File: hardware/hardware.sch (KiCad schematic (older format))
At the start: 38 parts, among them J1 USB_B_Micro, J2 Breakout, Q1 FS8205, U1 USBLC6-2, U2 PIC18F45K50_QFP, U3 LM317A, U4 DW01+G, U5 TP4056

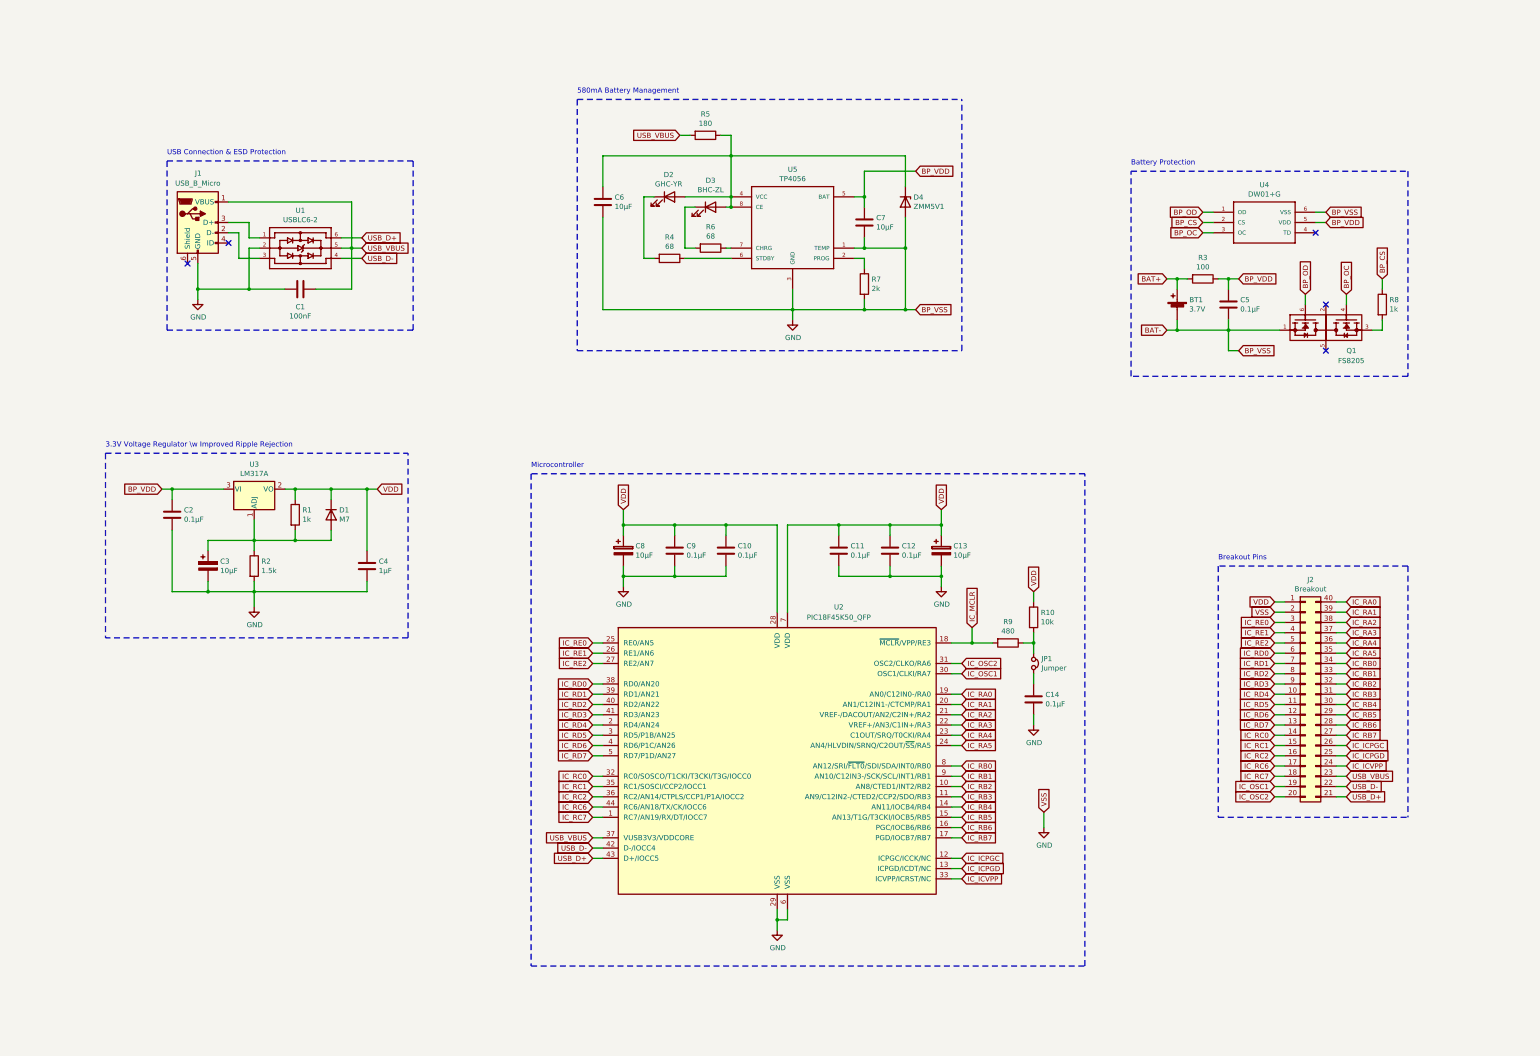
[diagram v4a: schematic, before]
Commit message: Assigned footprints to the project.
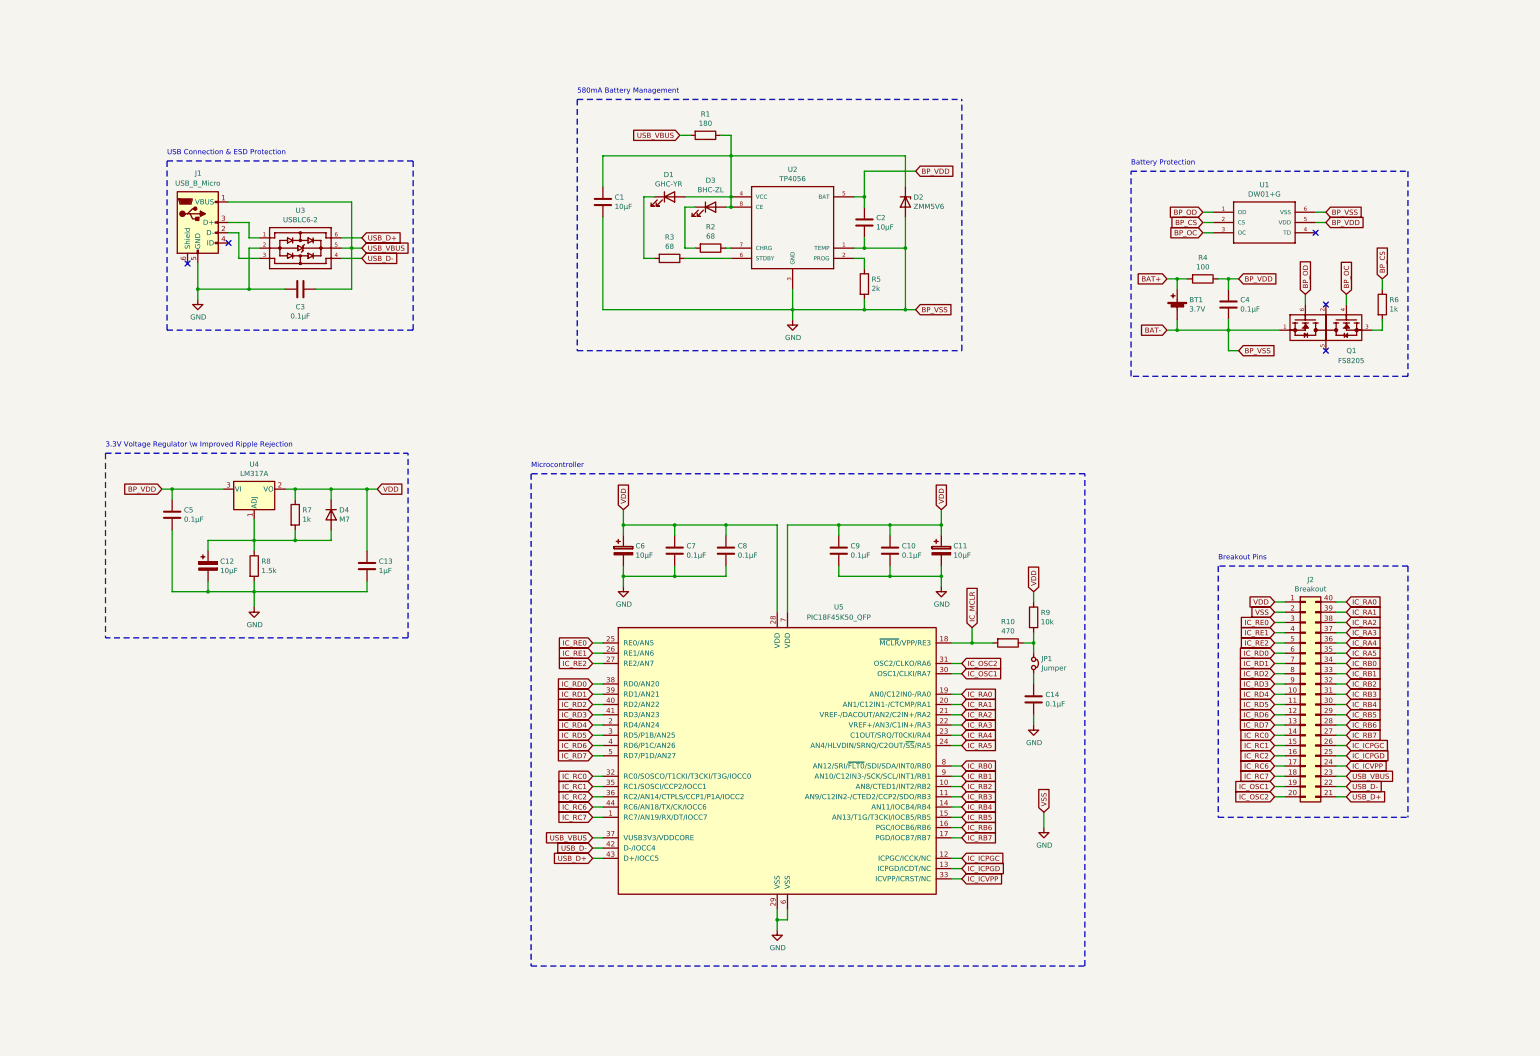
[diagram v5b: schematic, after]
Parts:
- BT1: footprint (none) -> Connector_PinHeader_2.54mm:PinHeader_1x02_P2.54mm_Horizontal
- C1: renamed from C6; footprint (none) -> Capacitor_SMD:C_0603_1608Metric_Pad1.05x0.95mm_HandSolder
- C10: renamed from C12; footprint (none) -> Capacitor_SMD:C_0603_1608Metric_Pad1.05x0.95mm_HandSolder
- C11: renamed from C13; footprint (none) -> Capacitor_SMD:C_0603_1608Metric_Pad1.05x0.95mm_HandSolder
- C12: renamed from C3; footprint (none) -> Capacitor_SMD:C_0603_1608Metric_Pad1.05x0.95mm_HandSolder
- C13: renamed from C4; footprint (none) -> Capacitor_SMD:C_0603_1608Metric_Pad1.05x0.95mm_HandSolder
- C14: footprint (none) -> Capacitor_SMD:C_0603_1608Metric_Pad1.05x0.95mm_HandSolder
- C2: renamed from C7; footprint (none) -> Capacitor_SMD:C_0603_1608Metric_Pad1.05x0.95mm_HandSolder
- C3: renamed from C1; value 100nF -> 0.1μF; footprint (none) -> Capacitor_SMD:C_0603_1608Metric_Pad1.05x0.95mm_HandSolder
- C4: renamed from C5; footprint (none) -> Capacitor_SMD:C_0603_1608Metric_Pad1.05x0.95mm_HandSolder
- C5: renamed from C2; footprint (none) -> Capacitor_SMD:C_0603_1608Metric_Pad1.05x0.95mm_HandSolder
- C6: renamed from C8; footprint (none) -> Capacitor_SMD:C_0603_1608Metric_Pad1.05x0.95mm_HandSolder
- C7: renamed from C9; footprint (none) -> Capacitor_SMD:C_0603_1608Metric_Pad1.05x0.95mm_HandSolder
- C8: renamed from C10; footprint (none) -> Capacitor_SMD:C_0603_1608Metric_Pad1.05x0.95mm_HandSolder
- C9: renamed from C11; footprint (none) -> Capacitor_SMD:C_0603_1608Metric_Pad1.05x0.95mm_HandSolder
- D1: renamed from D2; footprint (none) -> LED_SMD:LED_0603_1608Metric_Pad1.05x0.95mm_HandSolder
- D2: renamed from D4; value ZMM5V1 -> ZMM5V6
- D3: footprint (none) -> LED_SMD:LED_0603_1608Metric_Pad1.05x0.95mm_HandSolder
- D4: renamed from D1; footprint (none) -> Diode_SMD:D_MiniMELF_Handsoldering
- J1: footprint (none) -> Connector_USB:USB_Micro-B_Molex_47346-0001
- J2: footprint (none) -> Connector_PinHeader_2.54mm:PinHeader_2x20_P2.54mm_Vertical
- JP1: footprint (none) -> Connector_PinHeader_2.54mm:PinHeader_1x02_P2.54mm_Vertical
- R1: renamed from R5; footprint (none) -> Resistor_SMD:R_0603_1608Metric_Pad1.05x0.95mm_HandSolder
- R10: renamed from R9; value 480 -> 470; footprint (none) -> Resistor_SMD:R_0603_1608Metric_Pad1.05x0.95mm_HandSolder
- R2: renamed from R6; footprint (none) -> Resistor_SMD:R_0603_1608Metric_Pad1.05x0.95mm_HandSolder
- R3: renamed from R4; footprint (none) -> Resistor_SMD:R_0603_1608Metric_Pad1.05x0.95mm_HandSolder
- R4: renamed from R3; footprint (none) -> Resistor_SMD:R_0603_1608Metric_Pad1.05x0.95mm_HandSolder
- R5: renamed from R7; footprint (none) -> Resistor_SMD:R_0603_1608Metric_Pad1.05x0.95mm_HandSolder
- R6: renamed from R8; footprint (none) -> Resistor_SMD:R_0603_1608Metric_Pad1.05x0.95mm_HandSolder
- R7: renamed from R1; footprint (none) -> Resistor_SMD:R_0603_1608Metric_Pad1.05x0.95mm_HandSolder
- R8: renamed from R2; footprint (none) -> Resistor_SMD:R_0603_1608Metric_Pad1.05x0.95mm_HandSolder
- R9: renamed from R10; footprint (none) -> Resistor_SMD:R_0603_1608Metric_Pad1.05x0.95mm_HandSolder
- renumbered U4 to U1, U5 to U2, U1 to U3, U3 to U4, U2 to U5

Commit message: MAX2871 datasheet & footprint.
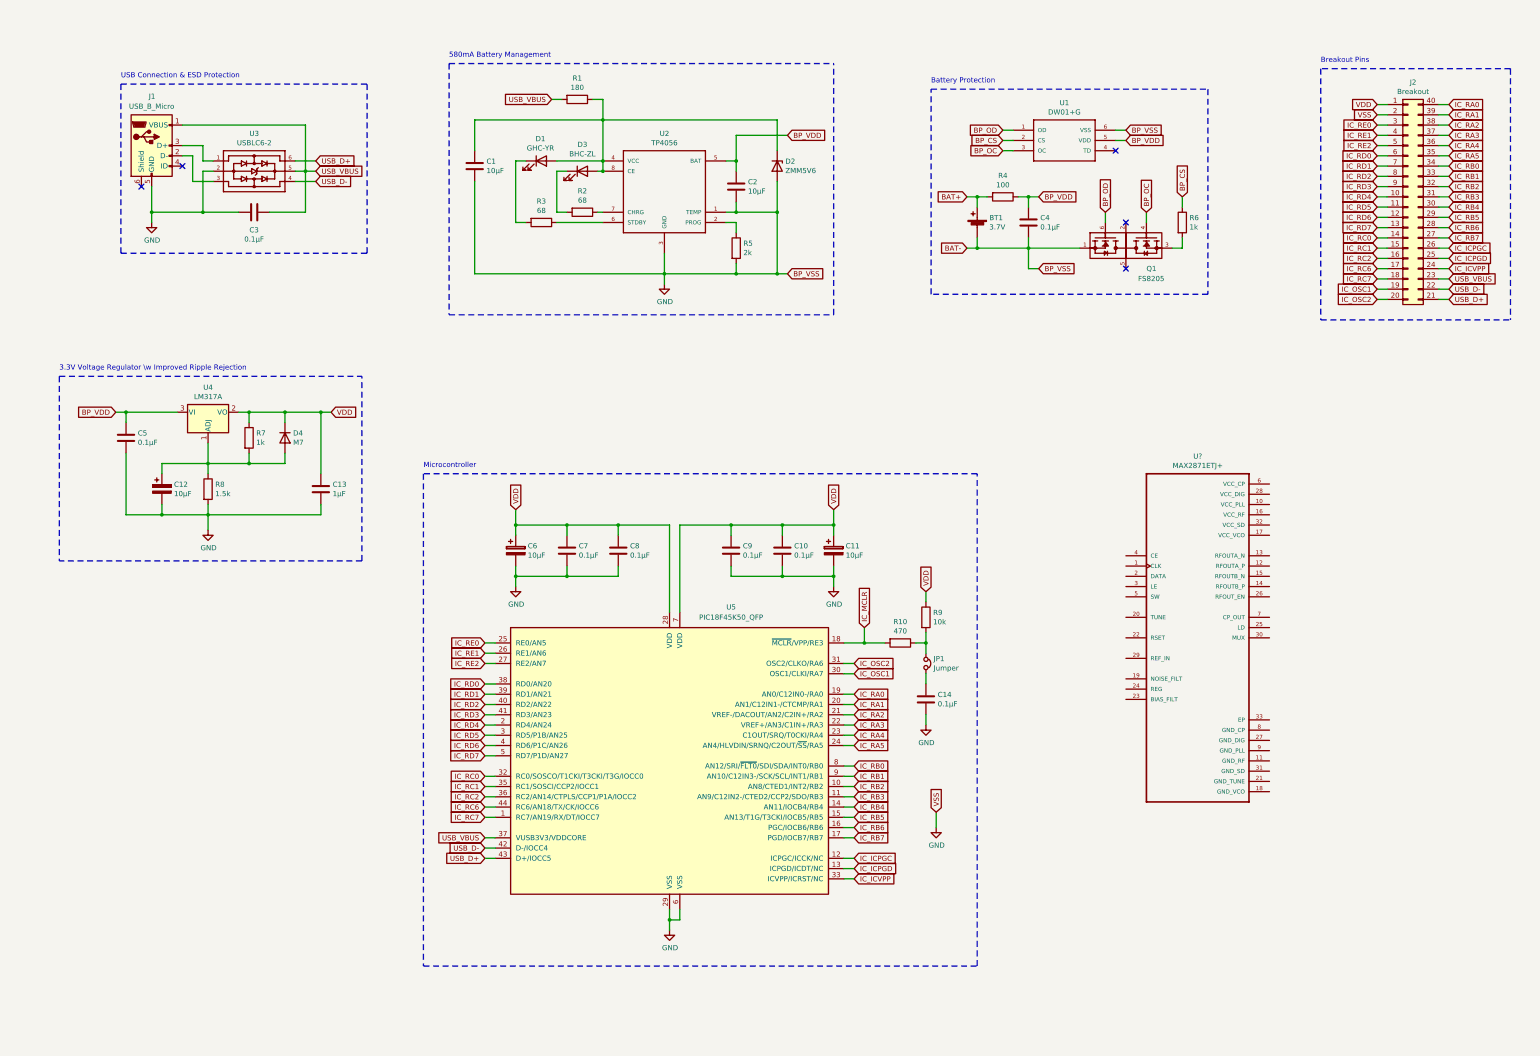
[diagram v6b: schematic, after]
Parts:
- added U?: MAX2871ETJ+, QFN50P500X500X80-33N, symbol Missing:MAX2871ETJ+
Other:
- moved on the sheet: BT1, C1, C10, C11, C12, C13, C14, C2, C3, C4, C5, C6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

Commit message: Compacted schematics.
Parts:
- added J3: Conn_Coaxial, symbol Connector:Conn_Coaxial
- gave numbers to parts that had none: 1
- renumbered C4 to C1, C8 to C10, C9 to C11, C10 to C12, C11 to C13, C3 to C2, C5 to C3, C1 to C4, C2 to C5, C12 to C6, C13 to C7, C6 to C8, C7 to C9, D4 to D1, D1 to D2, D2 to D3, D3 to D4, R4 to R1, R6 to R2, R1 to R3, R7 to R4, R8 to R5, R2 to R6, R3 to R7, R5 to R8, U3 to U2, U4 to U3, U2 to U4, U5 to U6
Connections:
- net IC_MCLR: now also J2.23 (Pin_23)
- net USB_VBUS: no longer J2.23 (Pin_23)
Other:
- moved on the sheet: BT1, C1, C10, C11, C12, C13, C14, C2, C3, C4, C5, C6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

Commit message: 50 MHz reference.
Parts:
- removed J2: Breakout, Connector_PinHeader_2.54mm:PinHeader_2x20_P2.54mm_Vertical, symbol Connector_Generic:Conn_02x20_Counter_Clockwise
- added C17, C18: 0.1μF, Capacitor_SMD:C_0603_1608Metric_Pad1.05x0.95mm_HandSolder, symbol Device:C
- added C4, C5, C6: 1μF, Capacitor_SMD:C_0603_1608Metric_Pad1.05x0.95mm_HandSolder, symbol Device:C
- added J3: Breakout, Connector_PinSocket_2.54mm:PinSocket_1x18_P2.54mm_Vertical, symbol Connector_Generic:Conn_02x19_Top_Bottom
- added R9: 1m, Resistor_SMD:R_0603_1608Metric_Pad1.05x0.95mm_HandSolder, symbol Device:R
- added X1: SG-310SCF, Crystal:Crystal_SMD_3225-4Pin_3.2x2.5mm_HandSoldering, symbol Missing:SG-310SCF
- U3: renamed from U5; footprint QFN50P500X500X80-33N -> (none)
- renumbered C7 to C10, C8 to C11, C9 to C12, C10 to C13, C11 to C14, C12 to C15, C13 to C16, C14 to C19, C4 to C7, C5 to C8, C6 to C9, J3 to J2, R9 to R10, R10 to R11, U3 to U4, U4 to U5
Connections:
- net GND: now also C18.2, C4.2, C5.2, C6.2, J3.20 (Pin_20), R9.2, X1.2 (GND)
- net IC_ICPGC: now also J3.35 (Pin_35)
- net IC_ICPGD: now also J3.36 (Pin_36)
- net IC_ICVPP: now also J3.37 (Pin_37)
- net IC_MCLR: now also J3.38 (Pin_38)
- net IC_OSC1: now also J3.18 (Pin_18)
- net IC_OSC2: now also J3.19 (Pin_19)
- net IC_RA0: now also J3.21 (Pin_21)
- net IC_RA1: now also J3.22 (Pin_22)
- net IC_RA2: now also J3.23 (Pin_23)
- net IC_RA3: now also J3.24 (Pin_24)
- net IC_RA4: now also J3.25 (Pin_25)
- net IC_RA5: now also J3.26 (Pin_26)
- net IC_RB0: now also J3.27 (Pin_27)
- net IC_RB1: now also J3.28 (Pin_28)
- net IC_RB2: now also J3.29 (Pin_29)
- net IC_RB3: now also J3.30 (Pin_30)
- net IC_RB4: now also J3.31 (Pin_31)
- net IC_RB5: now also J3.32 (Pin_32)
- net IC_RB6: now also J3.33 (Pin_33)
- net IC_RB7: now also J3.34 (Pin_34)
- net IC_RC0: now also J3.13 (Pin_13)
- net IC_RC1: now also J3.14 (Pin_14)
- net IC_RC2: now also J3.15 (Pin_15)
- net IC_RC6: now also J3.16 (Pin_16)
- net IC_RC7: now also J3.17 (Pin_17)
- net IC_RD0: now also J3.5 (Pin_5)
- net IC_RD1: now also J3.6 (Pin_6)
- net IC_RD2: now also J3.7 (Pin_7)
- net IC_RD3: now also J3.8 (Pin_8)
- net IC_RD4: now also J3.9 (Pin_9)
- net IC_RD5: now also J3.10 (Pin_10)
- net IC_RD6: now also J3.11 (Pin_11)
- net IC_RD7: now also J3.12 (Pin_12)
- net IC_RE0: now also J3.2 (Pin_2)
- net IC_RE1: now also J3.3 (Pin_3)
- net IC_RE2: now also J3.4 (Pin_4)
- net VDD: now also C18.1, J3.1 (Pin_1), X1.1 (ST), X1.4 (VCC)
- net at U3.19 (NOISE_FILT): now also C4.1
- net at U3.23 (BIAS_FILT): now also C6.1
- net at U3.24 (REG): now also C5.1
- net RF_REF: now reaches U3.29 (REF_IN)
- net RF_REF: now also C17.2, R9.1
- new net: C17.1, X1.3 (OUT)
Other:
- note added: "50 MHz Reference"
- moved on the sheet: J2, U3
